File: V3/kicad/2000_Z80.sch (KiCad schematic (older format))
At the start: 1 part, among them X2000 ACO-10.000MHz

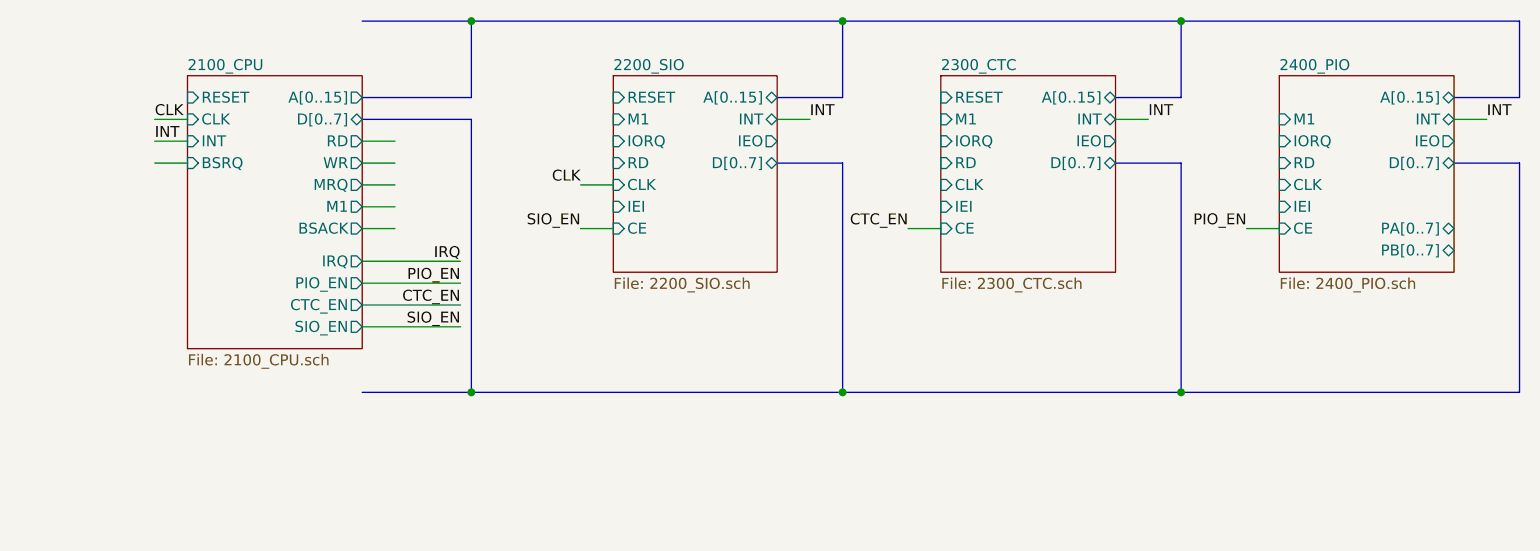
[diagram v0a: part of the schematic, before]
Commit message: probably going to split into two boards
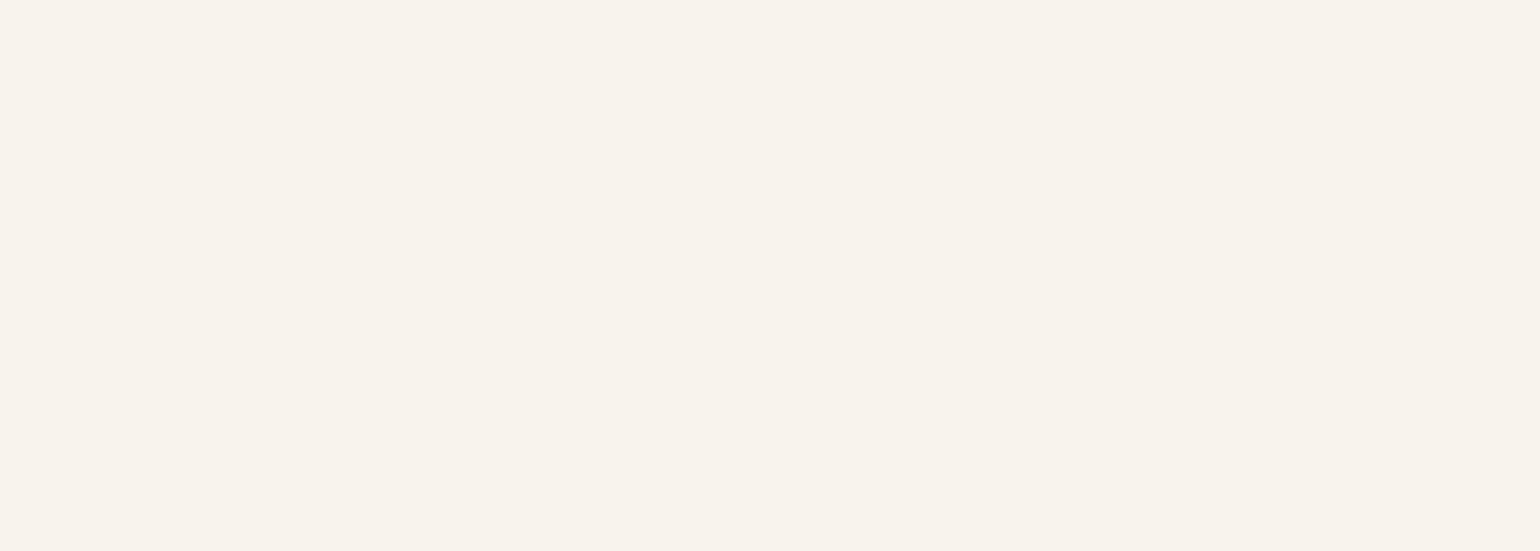
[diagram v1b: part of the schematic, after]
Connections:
- net labels removed: CTC_EN, INT, IRQ, PIO_EN, SIO_EN
- wire segments 31 -> 12
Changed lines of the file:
@@
 $Descr A4 11693 8268
 encoding utf-8
-Sheet 3 16
+Sheet 3 7
 Title ""
 Date ""
@@
 CLK
 $Sheet
-S 5300 -1950 750  900
-U 61EFA1CE
-F0 "2200_SIO" 50
-F1 "2200_SIO.sch" 50
-F2 "RESET" I L 5300 -1850 50
-F3 "M1" I L 5300 -1750 50
-F4 "IORQ" I L 5300 -1650 50
-F5 "RD" I L 5300 -1550 50
-F6 "CLK" I L 5300 -1450 50
-F7 "INT" T R 6050 -1750 50
-F8 "IEI" I L 5300 -1350 50
-F9 "IEO" O R 6050 -1650 50
-F10 "CE" I L 5300 -1250 50
-F11 "D[0..7]" B R 6050 -1550 50
-F12 "A[0..15]" B R 6050 -1850 50
-$EndSheet
-Wire Wire Line
-	4150 -1650 4300 -1650
-Wire Wire Line
-	4150 -1550 4300 -1550
-Wire Wire Line
-	4150 -1450 4300 -1450
-Wire Wire Line
-	3350 -1750 3200 -1750
-Wire Wire Line
-	3350 -1650 3200 -1650
-Wire Wire Line
-	3350 -1550 3200 -1550
-Text Label 3200 -1750 0    50   ~ 0
-CLK
-Wire Wire Line
-	5300 -1450 5150 -1450
-Text Label 5150 -1450 2    50   ~ 0
-CLK
-Text Label 3200 -1650 0    50   ~ 0
-INT
-Wire Wire Line
-	6200 -1750 6050 -1750
-Text Label 6200 -1750 0    50   ~ 0
-INT
-Wire Bus Line
-	6350 -1850 6350 -2200
-Wire Bus Line
-	4650 -1850 4650 -2200
-Wire Bus Line
-	6050 -1850 6350 -1850
-Wire Bus Line
-	6350 -1550 6050 -1550
-$Sheet
-S 6800 -1950 800  900
-U 61EEEF32
-F0 "2300_CTC" 50
-F1 "2300_CTC.sch" 50
-F2 "D[0..7]" B R 7600 -1550 50
-F3 "IEO" O R 7600 -1650 50
-F4 "INT" T R 7600 -1750 50
-F5 "A[0..15]" B R 7600 -1850 50
-F6 "CLK" I L 6800 -1450 50
-F7 "RESET" I L 6800 -1850 50
-F8 "M1" I L 6800 -1750 50
-F9 "IORQ" I L 6800 -1650 50
-F10 "RD" I L 6800 -1550 50
-F11 "IEI" I L 6800 -1350 50
-F12 "CE" I L 6800 -1250 50
-$EndSheet
-Wire Bus Line
-	7600 -1850 7900 -1850
-Wire Bus Line
-	7900 -1850 7900 -2200
-Wire Bus Line
-	7900 -1550 7600 -1550
-Wire Wire Line
-	7750 -1750 7600 -1750
-Text Label 7750 -1750 0    50   ~ 0
-INT
-Wire Bus Line
-	4150 -1750 4650 -1750
-Connection ~ 4650 -2200
-Wire Bus Line
-	4150 -2200 4650 -2200
-Wire Bus Line
-	4150 -1850 4650 -1850
-$Sheet
-S 8350 -1950 800  900
-U 61F73F94
-F0 "2400_PIO" 50
-F1 "2400_PIO.sch" 50
-F2 "M1" I L 8350 -1750 50
-F3 "IORQ" I L 8350 -1650 50
-F4 "RD" I L 8350 -1550 50
-F5 "IEI" I L 8350 -1350 50
-F6 "CE" I L 8350 -1250 50
-F7 "CLK" I L 8350 -1450 50
-F8 "D[0..7]" B R 9150 -1550 50
-F9 "IEO" O R 9150 -1650 50
-F10 "INT" T R 9150 -1750 50
-F11 "A[0..15]" B R 9150 -1850 50
-F12 "PA[0..7]" B R 9150 -1250 50
-F13 "PB[0..7]" B R 9150 -1150 50
-$EndSheet
-Wire Bus Line
-	9150 -1850 9450 -1850
-Wire Bus Line
-	9450 -1850 9450 -2200
-Wire Bus Line
-	9150 -1550 9450 -1550
-Wire Wire Line
-	9300 -1750 9150 -1750
-Text Label 9300 -1750 0    50   ~ 0
-INT
-Wire Bus Line
-	4150 -500 4650 -500
-Wire Bus Line
-	7900 -1550 7900 -500
-Wire Bus Line
-	9450 -1550 9450 -500
-Wire Bus Line
-	6350 -1550 6350 -500
-Wire Bus Line
-	4650 -1750 4650 -500
-Connection ~ 4650 -500
-Text Label 4600 -1000 2    50   ~ 0
-PIO_EN
-Text Label 4600 -900 2    50   ~ 0
-CTC_EN
-Text Label 4600 -800 2    50   ~ 0
-SIO_EN
-Wire Wire Line
-	8350 -1250 8200 -1250
-Wire Wire Line
-	6800 -1250 6650 -1250
-Wire Wire Line
-	5300 -1250 5150 -1250
-Text Label 8200 -1250 2    50   ~ 0
-PIO_EN
-Text Label 6650 -1250 2    50   ~ 0
-CTC_EN
-Text Label 5150 -1250 2    50   ~ 0
-SIO_EN
-Connection ~ 7900 -2200
-Connection ~ 7900 -500
-Connection ~ 6350 -2200
-Wire Bus Line
-	6350 -2200 7900 -2200
-Connection ~ 6350 -500
-Wire Bus Line
-	6350 -500 7900 -500
-Wire Bus Line
-	4650 -2200 6350 -2200
-Wire Bus Line
-	4650 -500 6350 -500
-Wire Bus Line
-	7900 -2200 9450 -2200
-Wire Bus Line
-	7900 -500 9450 -500
-Wire Wire Line
-	4150 -1000 4600 -1000
-Wire Wire Line
-	4150 -900 4600 -900
-Wire Wire Line
-	4150 -800 4600 -800
-$Sheet
-S 3350 -1950 800  1250
-U 61F0BDAE
-F0 "2100_CPU" 50
-F1 "2100_CPU.sch" 50
-F2 "RESET" I L 3350 -1850 50
-F3 "A[0..15]" O R 4150 -1850 50
-F4 "D[0..7]" B R 4150 -1750 50
-F5 "RD" O R 4150 -1650 50
-F6 "WR" O R 4150 -1550 50
-F7 "MRQ" O R 4150 -1450 50
-F8 "CLK" I L 3350 -1750 50
-F9 "INT" I L 3350 -1650 50
-F10 "BSRQ" I L 3350 -1550 50
-F11 "SIO_EN" O R 4150 -800 50
-F12 "CTC_EN" O R 4150 -900 50
-F13 "PIO_EN" O R 4150 -1000 50
-F14 "IRQ" O R 4150 -1100 50
-F15 "M1" O R 4150 -1350 50
-F16 "BSACK" O R 4150 -1250 50
-$EndSheet
-Wire Wire Line
-	4150 -1100 4600 -1100
-Text Label 4600 -1100 2    50   ~ 0
-IRQ
-Wire Wire Line
-	4150 -1350 4300 -1350
-Wire Wire Line
-	4150 -1250 4300 -1250
-$Sheet
 S 4400 3300 900  1100

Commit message: Updated PCB files
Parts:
- removed X2000: ACO-10.000MHz, Oscillator:Oscillator_DIP-14, symbol Oscillator:ACO-xxxMHz
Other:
- note removed: "Some key signals need to be tied high during BUSASK"
- note removed: "This page has NOT been checked!"
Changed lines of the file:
@@
 $Descr A4 11693 8268
 encoding utf-8
-Sheet 3 7
+Sheet 3 9
 Title ""
 Date ""
@@
 Comment4 ""
 $EndDescr
-Text Notes 1150 7250 0    197  ~ 39
-This page has NOT been checked!
-$Comp
-L Oscillator:ACO-xxxMHz X2000
-U 1 1 61E80A40
-P 1900 3700
-F 0 "X2000" H 1557 3746 50  0000 R CNN
-F 1 "ACO-10.000MHz" H 1557 3655 50  0000 R CNN
-F 2 "Oscillator:Oscillator_DIP-14" H 2350 3350 50  0001 C CNN
-F 3 "http://www.conwin.com/datasheets/cx/cx030.pdf" H 1800 3700 50  0001 C CNN
-	1    1900 3700
-	1    0    0    -1
-$EndComp
-$Comp
-L power:+5V #PWR0108
-U 1 1 61E80A46
-P 1900 3400
-F 0 "#PWR0108" H 1900 3250 50  0001 C CNN
-F 1 "+5V" H 1915 3573 50  0000 C CNN
-F 2 "" H 1900 3400 50  0001 C CNN
-F 3 "" H 1900 3400 50  0001 C CNN
-	1    1900 3400
-	1    0    0    -1
-$EndComp
-$Comp
-L power:GND #PWR0109
-U 1 1 61E80A4C
-P 1900 4000
-F 0 "#PWR0109" H 1900 3750 50  0001 C CNN
-F 1 "GND" H 1905 3827 50  0000 C CNN
-F 2 "" H 1900 4000 50  0001 C CNN
-F 3 "" H 1900 4000 50  0001 C CNN
-	1    1900 4000
-	1    0    0    -1
-$EndComp
-Wire Wire Line
-	2200 3700 2450 3700
-Text Label 2450 3700 0    50   ~ 0
-CLK
-$Sheet
-S 4400 3300 900  1100
-U 61EBDADB
-F0 "2100_ALTCPU" 50
-F1 "2100_ALTCPU.sch" 50
-F2 "RESET" I L 4400 3400 50
-F3 "BUSRQ" I L 4400 3500 50
-F4 "INT" I L 4400 3600 50
-F5 "D[0..7]" B R 5300 3500 50
-F6 "A[0..19]" T R 5300 3400 50
-F7 "MREQ" O R 5300 3700 50
-F8 "BUSAK" O R 5300 3900 50
-F9 "ST" O R 5300 4200 50
-F10 "M1" O R 5300 4300 50
-F11 "IORQ" O R 5300 4000 50
-F12 "RD" O R 5300 4100 50
-F13 "WR" O R 5300 3800 50
-F14 "CLK" I L 4400 3700 50
-$EndSheet
-$Sheet
-S 6450 3300 850  1150
-U 61F28B7D
-F0 "2200_PERP_ALT" 50
-F1 "2200_PERP_ALT.sch" 50
-F2 "RESET" I L 6450 3700 50
-F3 "A[0..19]" I L 6450 3400 50
-F4 "D[0..7]" B L 6450 3500 50
-F5 "RW" I L 6450 3800 50
-F6 "CLK" I L 6450 3900 50
-F7 "CS" I L 6450 4000 50
-$EndSheet
-Wire Wire Line
-	6450 3900 6200 3900
-Text Label 6200 3900 0    50   ~ 0
-CLK
-Text HLabel 5650 4300 2    50   Output ~ 0
-M1
-Text HLabel 5650 4200 2    50   Output ~ 0
-ST
-Text HLabel 5650 4100 2    50   Output ~ 0
-RD
-Text HLabel 5650 4000 2    50   Output ~ 0
-IORQ
-Text HLabel 5650 3900 2    50   Output ~ 0
-BUSACK
-Text HLabel 5650 3800 2    50   Output ~ 0
-WR
-Text HLabel 5650 3700 2    50   Output ~ 0
-MREQ
-Wire Wire Line
-	5300 3900 5650 3900
-Wire Wire Line
-	5300 3800 5650 3800
-Wire Wire Line
-	5300 3700 5650 3700
-Wire Wire Line
-	5300 4000 5650 4000
-Wire Wire Line
-	5300 4100 5650 4100
-Wire Wire Line
-	5300 4200 5650 4200
-Wire Wire Line
-	5300 4300 5650 4300
-Text Label 5450 4000 0    50   ~ 0
-IORQ
-Wire Wire Line
-	6200 3800 6450 3800
-Wire Wire Line
-	6200 4000 6450 4000
-Text Label 6200 4000 0    50   ~ 0
-IORQ
-Text Label 5500 3800 0    50   ~ 0
-WR
-Text Label 6200 3800 0    50   ~ 0
-WR
 Wire Bus Line
 	5300 3400 5400 3400
@@
 Text HLabel 5150 3150 0    50   3State ~ 0
 D[0..7]
-Text Notes 4900 4850 0    50   ~ 0
-Some key signals need to be tied high during BUSASK
 Wire Wire Line
-	4400 3700 4150 3700
-Text Label 4150 3700 0    50   ~ 0
-CLK
-Text HLabel 4400 3400 0    50   Input ~ 0
-RESET
-Text HLabel 6450 3700 0    50   Input ~ 0
-RESET
+	5300 3600 6450 3600
+$Sheet
+S 6450 3300 850  1150
+U 61F28B7D
+F0 "2200_PERP_ALT" 50
+F1 "2200_PERP_ALT.sch" 50
+F2 "A[0..19]" I L 6450 3400 50
+F3 "D[0..7]" B L 6450 3500 50
+F4 "CLK" I L 6450 3600 50
+F5 "CS" I L 6450 3900 50
+F6 "IORQ" I L 6450 4000 50
+F7 "RD" I L 6450 4100 50
+F8 "M1" I L 6450 4300 50
+F9 "INT" O L 6450 3800 50
+$EndSheet
+Wire Wire Line
+	5300 4000 6450 4000
+Wire Wire Line
+	5300 4300 6450 4300
+$Sheet
+S 4400 3300 900  1100
+U 61EBDADB
+F0 "2100_ALTCPU" 50
+F1 "2100_ALTCPU.sch" 50
+F2 "D[0..7]" B R 5300 3500 50
+F3 "A[0..19]" T R 5300 3400 50
+F4 "M1" O R 5300 4300 50
+F5 "IORQ" O R 5300 4000 50
+F6 "RD" O R 5300 4100 50
+F7 "PHI" O R 5300 3600 50
+F8 "ROM_CS" O L 4400 4000 50
+F9 "PIO_EN" O R 5300 3900 50
+F10 "MREAD" O L 4400 3900 50
+F11 "MWRITE" O L 4400 3800 50
+F12 "INT" I R 5300 3800 50
+F13 "H_RAM_CS" O L 4400 4100 50
+$EndSheet
+Wire Wire Line
+	5300 4100 6450 4100
+Wire Wire Line
+	5300 3900 6450 3900
+Text HLabel 4400 3800 0    50   Output ~ 0
+WRITE
+Text HLabel 4400 3900 0    50   Output ~ 0
+READ
+Text HLabel 4400 4000 0    50   Output ~ 0
+ROM_CS
+Text HLabel 4400 4100 0    50   Output ~ 0
+RAM_CS
+Wire Wire Line
+	6450 3800 5300 3800
 $EndSCHEMATC

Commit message: still trying to make routes work
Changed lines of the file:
@@
 $EndDescr
-Wire Bus Line
-	5300 3400 5400 3400
-Wire Bus Line
-	5400 3400 5400 3150
 Wire Bus Line
 	5400 3150 5150 3150
 Wire Bus Line
-	5300 3500 5500 3500
-Wire Bus Line
-	5500 3500 5500 3050
-Wire Bus Line
 	5500 3050 5150 3050
-Wire Bus Line
-	5500 3500 6450 3500
-Connection ~ 5500 3500
-Wire Bus Line
-	5400 3400 6450 3400
-Connection ~ 5400 3400
-Text HLabel 5150 3050 0    50   3State ~ 0
-A[0..19]
 Text HLabel 5150 3150 0    50   3State ~ 0
 D[0..7]
@@
 F1 "2100_ALTCPU.sch" 50
 F2 "D[0..7]" B R 5300 3500 50
-F3 "A[0..19]" T R 5300 3400 50
-F4 "M1" O R 5300 4300 50
-F5 "IORQ" O R 5300 4000 50
-F6 "RD" O R 5300 4100 50
-F7 "PHI" O R 5300 3600 50
-F8 "ROM_CS" O L 4400 4000 50
-F9 "PIO_EN" O R 5300 3900 50
-F10 "MREAD" O L 4400 3900 50
-F11 "MWRITE" O L 4400 3800 50
-F12 "INT" I R 5300 3800 50
-F13 "H_RAM_CS" O L 4400 4100 50
+F3 "M1" O R 5300 4300 50
+F4 "IORQ" O R 5300 4000 50
+F5 "RD" O R 5300 4100 50
+F6 "PHI" O R 5300 3600 50
+F7 "ROM_CS" O L 4400 4000 50
+F8 "PIO_EN" O R 5300 3900 50
+F9 "MREAD" O L 4400 3900 50
+F10 "MWRITE" O L 4400 3800 50
+F11 "INT" I R 5300 3800 50
+F12 "H_RAM_CS" O L 4400 4100 50
+F13 "A[0..19]" O R 5300 3400 50
 $EndSheet
 Wire Wire Line
@@
 Wire Wire Line
 	6450 3800 5300 3800
+Text HLabel 5150 3050 0    50   Output ~ 0
+A[0..19]
+Wire Bus Line
+	5300 3400 5500 3400
+Wire Bus Line
+	5300 3500 5400 3500
+Wire Bus Line
+	5400 3150 5400 3500
+Connection ~ 5400 3500
+Wire Bus Line
+	5400 3500 6450 3500
+Wire Bus Line
+	5500 3050 5500 3400
+Connection ~ 5500 3400
+Wire Bus Line
+	5500 3400 6450 3400
 $EndSCHEMATC

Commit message: More rearranging
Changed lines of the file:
@@
 F7 "ROM_CS" O L 4400 4000 50
 F8 "PIO_EN" O R 5300 3900 50
-F9 "MREAD" O L 4400 3900 50
-F10 "MWRITE" O L 4400 3800 50
-F11 "INT" I R 5300 3800 50
-F12 "H_RAM_CS" O L 4400 4100 50
-F13 "A[0..19]" O R 5300 3400 50
+F9 "INT" I R 5300 3800 50
+F10 "A[0..19]" O R 5300 3400 50
+F11 "RAM_CS" O L 4400 4100 50
+F12 "WR" O R 5300 4200 50
 $EndSheet
 Wire Wire Line
-	5300 4100 6450 4100
-Wire Wire Line
 	5300 3900 6450 3900
-Text HLabel 4400 3800 0    50   Output ~ 0
-WRITE
-Text HLabel 4400 3900 0    50   Output ~ 0
-READ
 Text HLabel 4400 4000 0    50   Output ~ 0
 ROM_CS
@@
 Wire Bus Line
 	5500 3400 6450 3400
+Text HLabel 5300 4200 2    50   Output ~ 0
+WR
+Text HLabel 5850 4200 2    50   Output ~ 0
+RD
+Wire Wire Line
+	5300 4100 5750 4100
+Wire Wire Line
+	5850 4200 5750 4200
+Wire Wire Line
+	5750 4200 5750 4100
+Connection ~ 5750 4100
+Wire Wire Line
+	5750 4100 6450 4100
 $EndSCHEMATC

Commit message: A lot of disorganized changes
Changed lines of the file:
@@
 $Descr A4 11693 8268
 encoding utf-8
-Sheet 3 8
+Sheet 3 7
 Title ""
 Date ""
@@
 Comment4 ""
 $EndDescr
-Wire Bus Line
-	5400 3150 5150 3150
-Wire Bus Line
-	5500 3050 5150 3050
-Text HLabel 5150 3150 0    50   3State ~ 0
+Text HLabel 5300 3500 2    50   3State ~ 0
 D[0..7]
-Wire Wire Line
-	5300 3600 6450 3600
-$Sheet
-S 6450 3300 850  1150
-U 61F28B7D
-F0 "2200_PERP_ALT" 50
-F1 "2200_PERP_ALT.sch" 50
-F2 "A[0..19]" I L 6450 3400 50
-F3 "D[0..7]" B L 6450 3500 50
-F4 "CLK" I L 6450 3600 50
-F5 "CS" I L 6450 3900 50
-F6 "IORQ" I L 6450 4000 50
-F7 "RD" I L 6450 4100 50
-F8 "M1" I L 6450 4300 50
-F9 "INT" O L 6450 3800 50
-$EndSheet
-Wire Wire Line
-	5300 4000 6450 4000
-Wire Wire Line
-	5300 4300 6450 4300
 $Sheet
 S 4400 3300 900  1100
@@
 F12 "WR" O R 5300 4200 50
 $EndSheet
-Wire Wire Line
-	5300 3900 6450 3900
 Text HLabel 4400 4000 0    50   Output ~ 0
 ROM_CS
 Text HLabel 4400 4100 0    50   Output ~ 0
 RAM_CS
-Wire Wire Line
-	6450 3800 5300 3800
-Text HLabel 5150 3050 0    50   Output ~ 0
+Text HLabel 5300 3400 2    50   Output ~ 0
 A[0..19]
-Wire Bus Line
-	5300 3400 5500 3400
-Wire Bus Line
-	5300 3500 5400 3500
-Wire Bus Line
-	5400 3150 5400 3500
-Connection ~ 5400 3500
-Wire Bus Line
-	5400 3500 6450 3500
-Wire Bus Line
-	5500 3050 5500 3400
-Connection ~ 5500 3400
-Wire Bus Line
-	5500 3400 6450 3400
 Text HLabel 5300 4200 2    50   Output ~ 0
 WR
-Text HLabel 5850 4200 2    50   Output ~ 0
+Text HLabel 5300 4100 2    50   Output ~ 0
 RD
-Wire Wire Line
-	5300 4100 5750 4100
-Wire Wire Line
-	5850 4200 5750 4200
-Wire Wire Line
-	5750 4200 5750 4100
-Connection ~ 5750 4100
-Wire Wire Line
-	5750 4100 6450 4100
 $EndSCHEMATC
